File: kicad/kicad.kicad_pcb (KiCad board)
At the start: 4 copper layers, 31.8 x 37.3 mm, 93 parts, among them J201 USB_C_Receptacle_USB2.0_16P, J301 BATTERY_CONN, J501 MOTOR_CONN, Q401 Si1308EDL, Q701 DMG1012T, SW101 PWR_SWITCH, SW601 BT1, SW602 BT3, SW603 BT2, SW604 BT4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

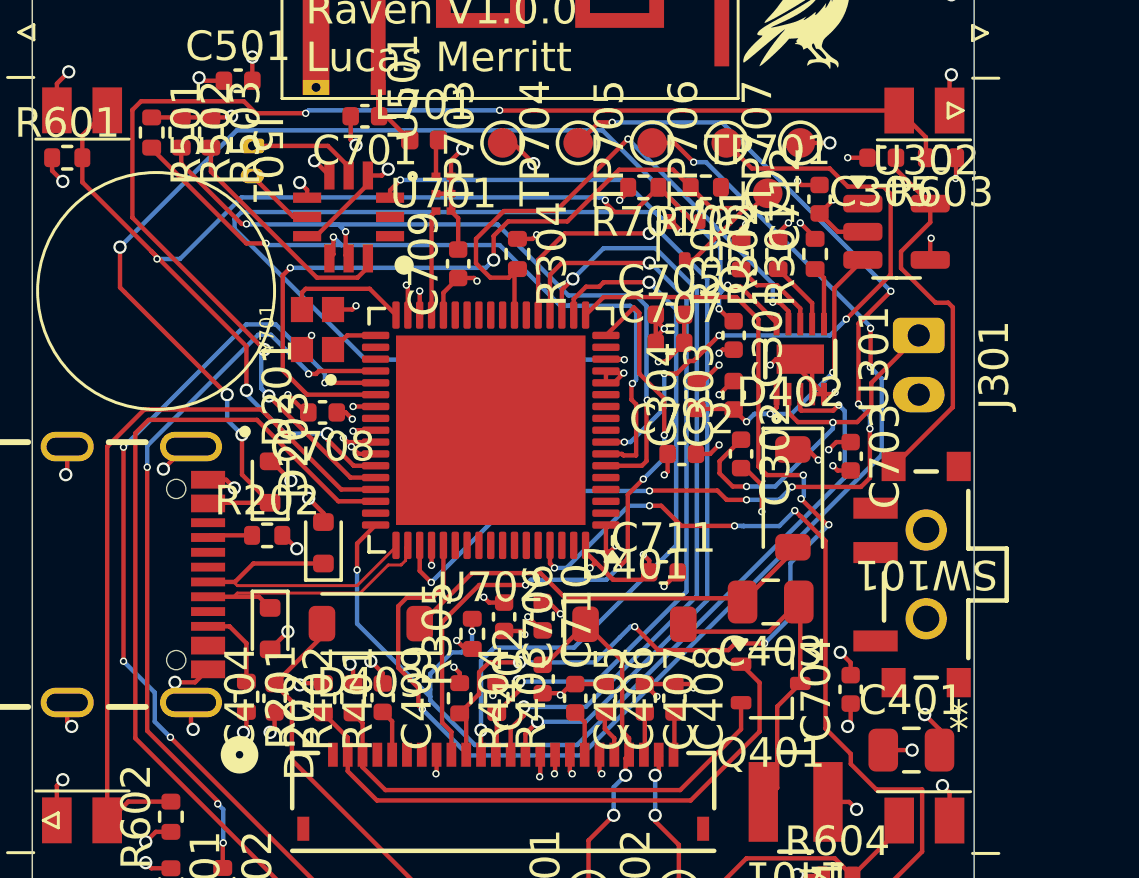
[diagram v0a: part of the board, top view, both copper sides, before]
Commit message: Fix bad connections
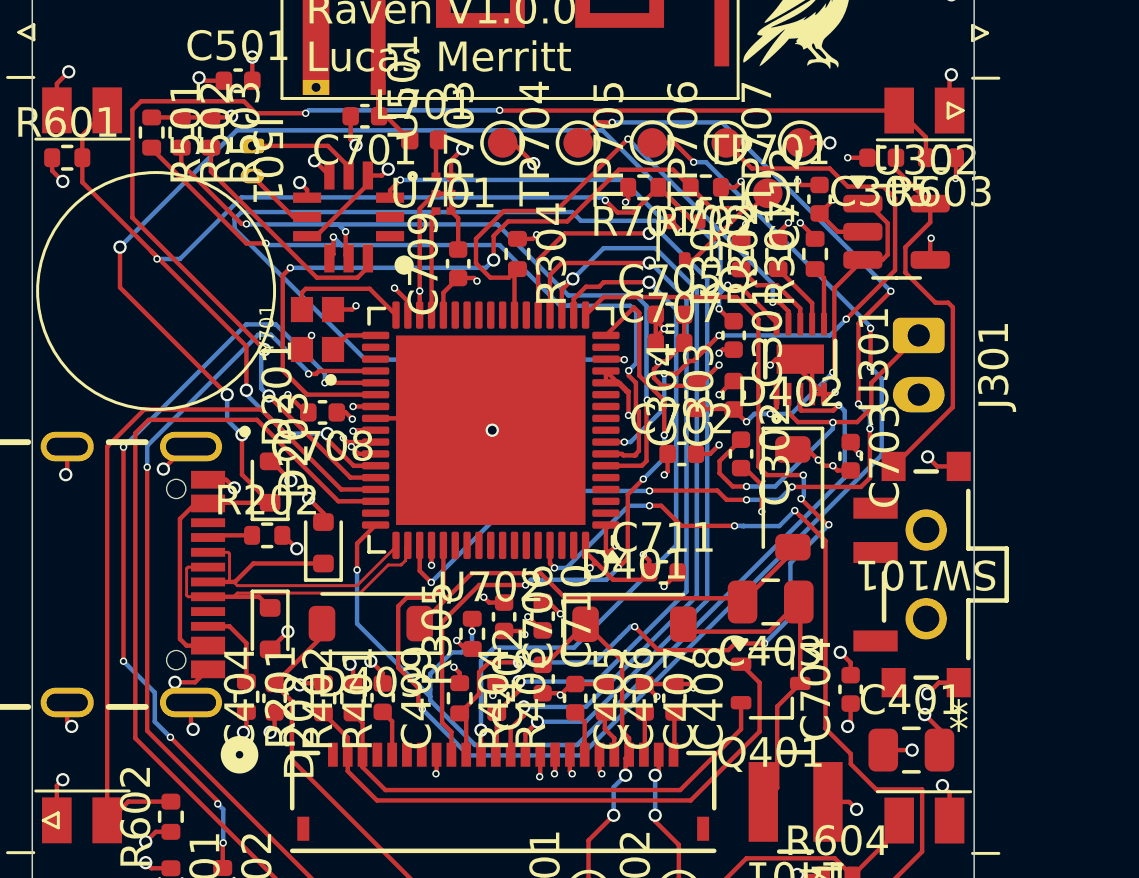
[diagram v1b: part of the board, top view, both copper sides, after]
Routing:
- net GND: track 72.3 -> 84.2 mm, vias 66 -> 68
- net VBUS: track 41.7 -> 48.0 mm
- net +3.3V: track 41.7 -> 45.0 mm, vias 36 -> 38
- net /Battery Management/SYS_T: track 11.0 -> 14.1 mm
- net /Microcontroller/D-: track 11.1 -> 13.5 mm
- net /Microcontroller/D+: track 9.97 -> 12.4 mm

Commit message: Begin EPD redo
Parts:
- EPD_FPC401: footprint Raven:CONN_F3311A7H121024E200_AMP -> Raven:CONN_F3311A7H121024E200_AMP_FACE_UP
- moved C706 19.1 mm to (161.4, 120.2)
- moved C710 19.0 mm to (162.6, 120.2)
- moved C711 17.2 mm to (164.5, 120.6)
- moved R401 15.2 mm to (151.5, 122.5), turned to 90 degrees
- moved R402 15.2 mm to (152.5, 122.5), turned to -90 degrees
- moved C408 12.4 mm to (135.9, 120.0)
- moved C409 12.2 mm to (150.4, 122.5), turned to 90 degrees
- moved R305 11.8 mm to (151.5, 112.0)
- moved C407 10.4 mm to (136.9, 120.0)
- moved TP401 8.90 mm to (153.9, 124.5)
- moved C406 8.00 mm to (137.9, 120.0)
- moved C403 6.92 mm to (144.6, 117.5)
- moved C405 6.01 mm to (138.9, 120.0)
- moved D401 5.40 mm to (141.6, 118.8), turned to 90 degrees
- moved L401 4.62 mm to (150.8, 119.4)
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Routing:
- net /Microcontroller/SWCLK: track 41.8 -> 0.00 mm, vias 4 -> 0
- net /Microcontroller/SWDIO: track 38.1 -> 0.00 mm, vias 8 -> 0
- net /Battery Management/STAT2: track 33.4 -> 0.00 mm, vias 3 -> 0
- net /E-Paper Display/MOSI: track 28.1 -> 0.00 mm, vias 2 -> 0
- net /E-Paper Display/CS_N: track 26.2 -> 0.00 mm, vias 2 -> 0
- net /E-Paper Display/SCK: track 26.1 -> 0.00 mm, vias 2 -> 0
- net /E-Paper Display/DC: track 24.1 -> 0.00 mm, vias 2 -> 0
- net /E-Paper Display/BUSY: track 22.5 -> 0.00 mm, vias 4 -> 0
- net /E-Paper Display/RES_N: track 33.9 -> 19.7 mm, vias 6 -> 2
- net /E-Paper Display/GDR: track 20.1 -> 6.08 mm
- net /E-Paper Display/PREVGH: track 12.2 -> 23.8 mm, vias 2 -> 0
- net +3.3V: track 45.0 -> 34.5 mm, vias 38 -> 29
- net /E-Paper Display/RESE: track 17.1 -> 9.18 mm
- net GND: track 84.2 -> 77.9 mm, vias 68 -> 63
- net Net-(D402-A): track 14.6 -> 9.40 mm
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
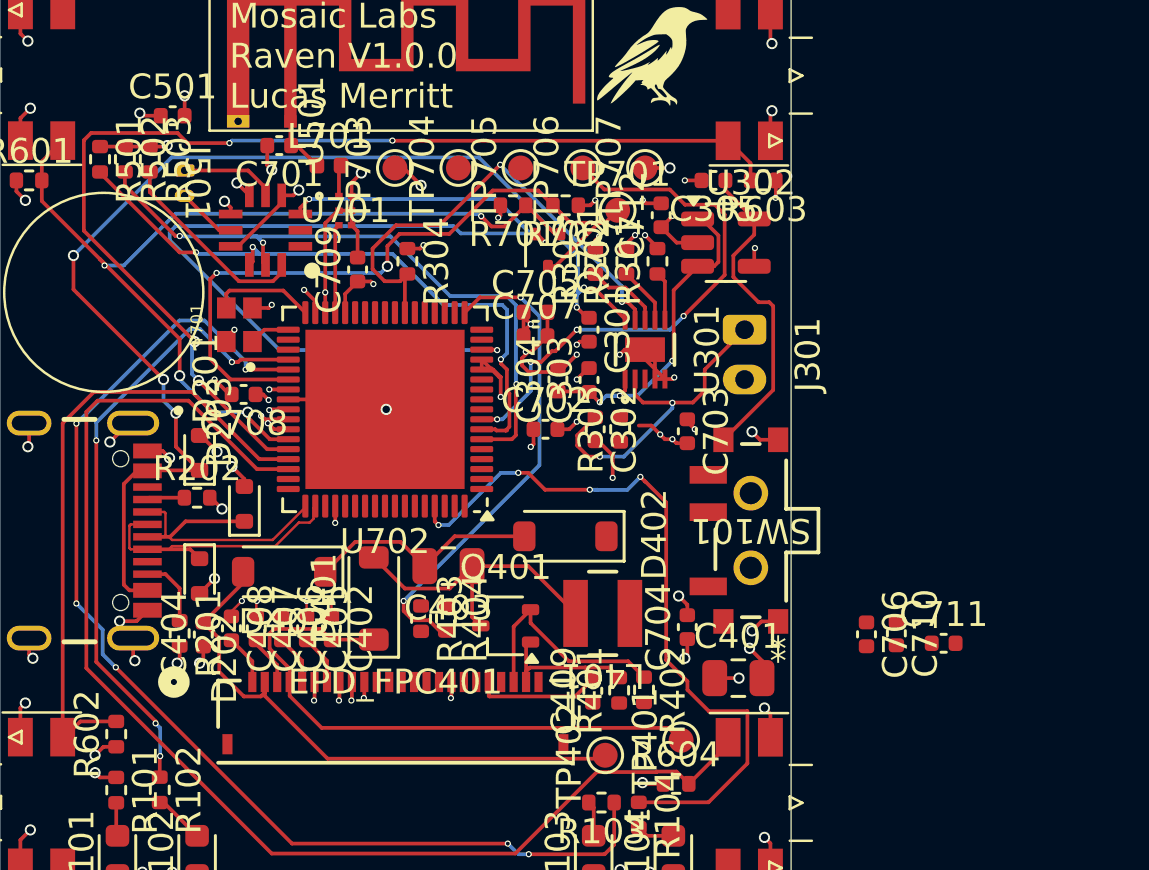
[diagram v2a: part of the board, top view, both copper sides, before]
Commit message: Finish flipping EPD
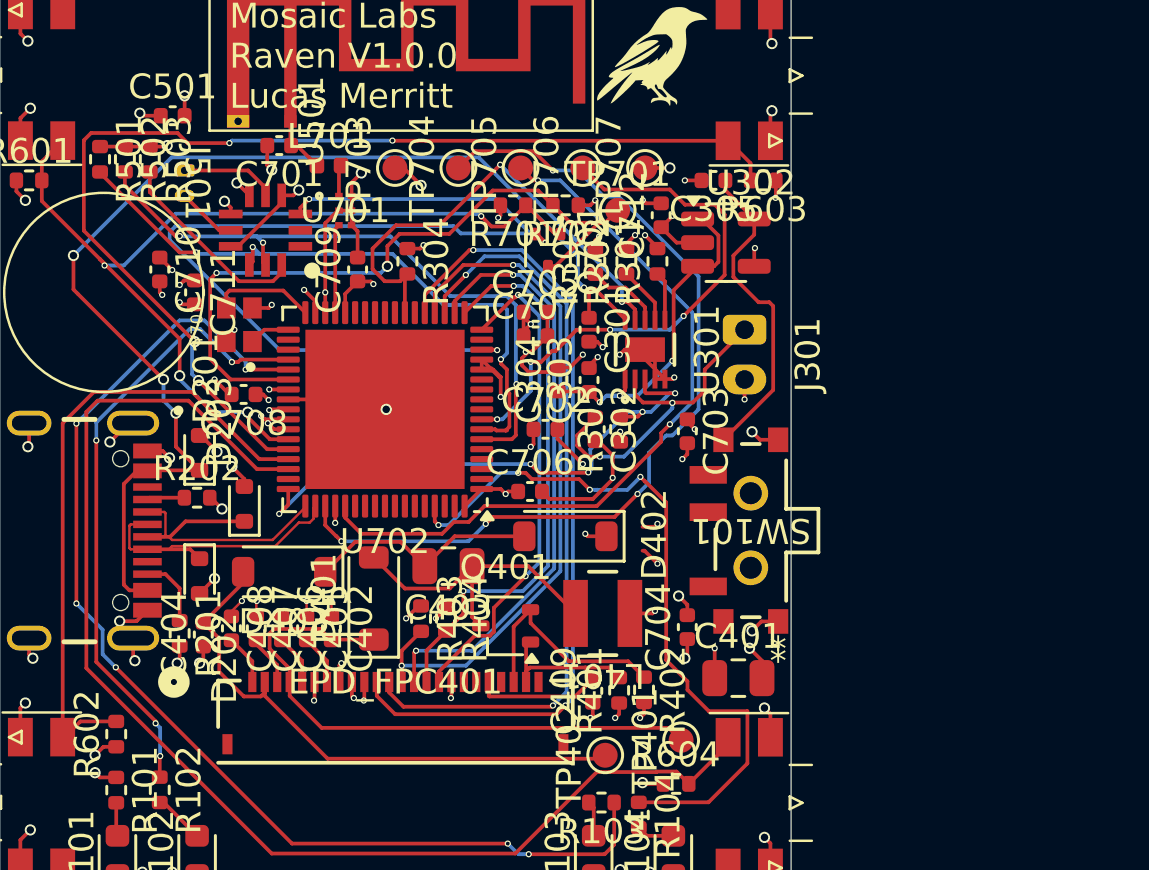
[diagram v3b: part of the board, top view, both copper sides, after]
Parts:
- moved C711 33.2 mm to (134.4, 106.5), turned to -90 degrees
- moved C710 33.0 mm to (133.0, 105.6)
- moved C706 14.7 mm to (147.9, 114.5), turned to 0 degrees
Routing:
- net /Microcontroller/SWDIO: track 0.00 -> 36.3 mm, vias 0 -> 4
- net /E-Paper Display/MOSI: track 0.00 -> 33.2 mm, vias 0 -> 2
- net /E-Paper Display/SCK: track 0.00 -> 30.6 mm, vias 0 -> 2
- net /Microcontroller/SWCLK: track 0.00 -> 30.0 mm, vias 0 -> 2
- net /E-Paper Display/CS_N: track 0.00 -> 28.6 mm, vias 0 -> 2
- net /E-Paper Display/DC: track 0.00 -> 24.1 mm, vias 0 -> 2
- net /Battery Management/STAT2: track 0.00 -> 22.6 mm, vias 0 -> 5
- net /E-Paper Display/BUSY: track 0.00 -> 20.0 mm, vias 0 -> 2
- net GND: track 77.9 -> 86.4 mm, vias 63 -> 70
- net +3.3V: track 34.5 -> 42.4 mm, vias 29 -> 37
- net /E-Paper Display/RES_N: track 19.7 -> 22.5 mm
- net VBUS: track 48.0 -> 47.6 mm, vias 5 -> 4

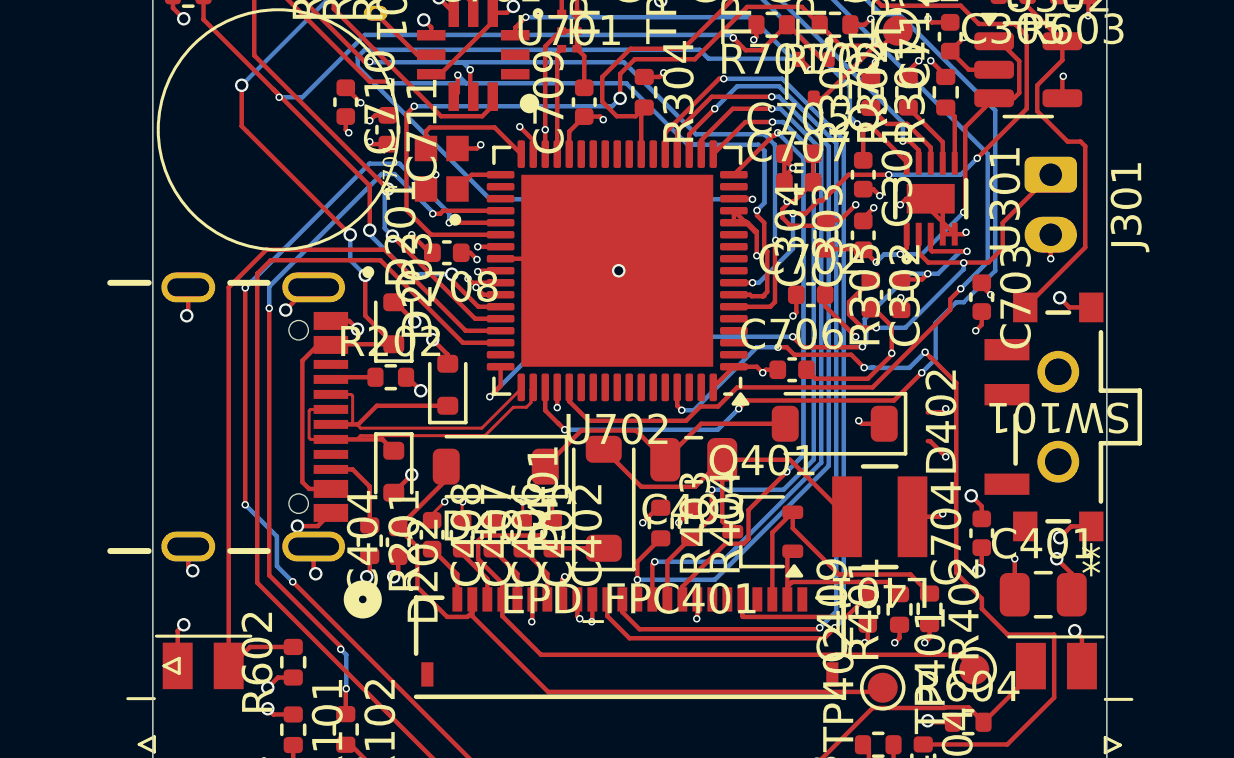
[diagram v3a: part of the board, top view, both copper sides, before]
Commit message: Fix DRC errors and vias
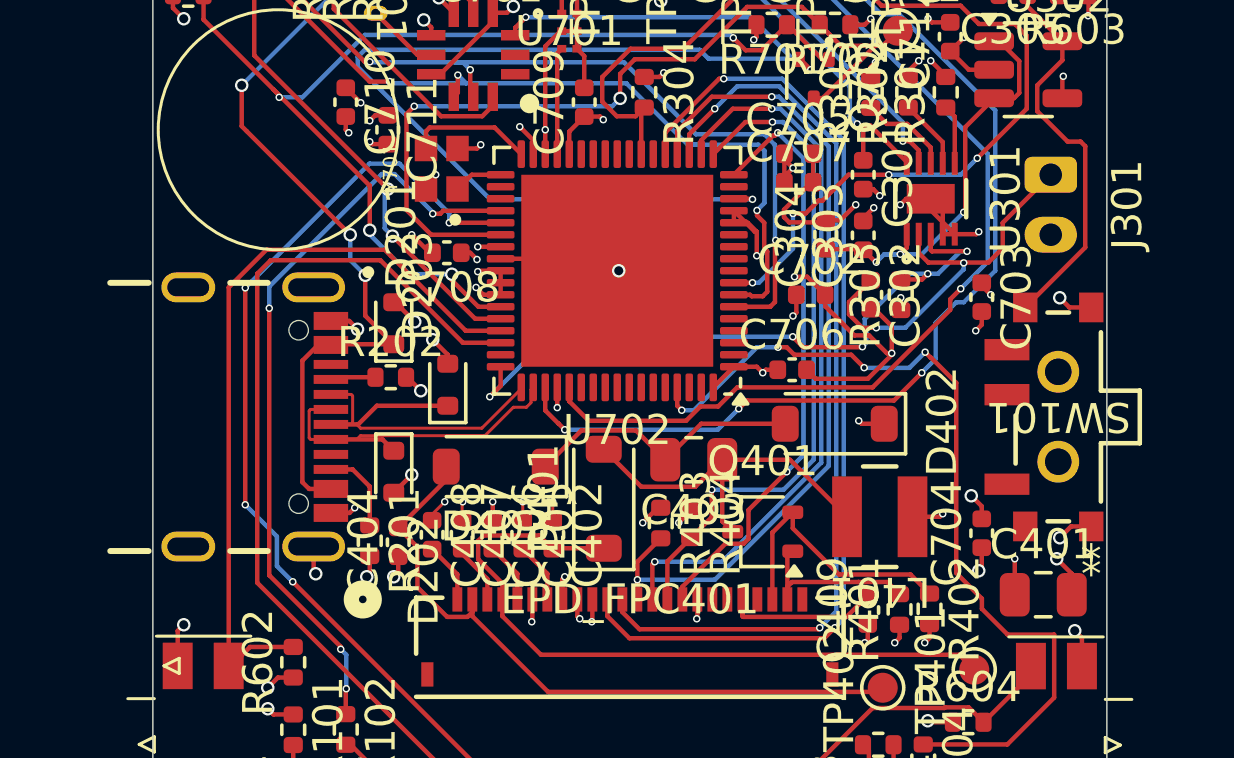
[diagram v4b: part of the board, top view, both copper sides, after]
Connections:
- AE701 pad 2: (no net) -> GND
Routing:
- net GND: track 86.4 -> 84.8 mm, vias 70 -> 65
- net +3.3V: track 42.4 -> 41.3 mm, vias 37 -> 35

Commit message: Finish silkscreen
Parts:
- removed TP301: BATTP_TEST, TestPoint:TestPoint_Pad_D1.0mm
- removed TP302: SYS_TEST, TestPoint:TestPoint_Pad_D1.0mm
- removed TP303: LDO_TEST, TestPoint:TestPoint_Pad_D1.0mm
- moved C711 20.5 mm to (152.3, 116.5)
- moved C710 17.1 mm to (134.3, 122.7)
- moved G*** 0.16 mm to (152.9, 97.1)
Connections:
- AE701 pad 2: GND -> (no net)
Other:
- board text added: "+ -"
- board text added: "0"
- board text added: "3V3"
- board text added: "CLK"
- board text added: "DIO"
- board text added: "GND"
- board text added: "Mosaic Labs Raven V2.0.0 Lucas Merritt"
- board text added: "NRST"
- board text added: "VGH"
- board text added: "VGL"
- board text removed: "Mosaic Labs Raven V1.0.0 Lucas Merritt"
